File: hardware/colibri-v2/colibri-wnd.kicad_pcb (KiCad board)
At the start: 4 copper layers, 120 x 120 mm, 527 parts, among them CN1 XT60-M, CN10 629_105_150_921, CN11 629_105_150_921, CN12 XT60-F, CN2 XT60-F, CN3 AS0B821-S78B-7H, CN4 HDMI_A, CN5 692_121_030_100, CN6 Wurth-68715014522-LCD, CN7 MOLEX_73366_0061, CN8 629_105_150_921, CN9 Wurth-68711814522, CON1 PJ-102AH, P1 CONN_02X10, P10 CONN_01X08, P11 CONN_01X03, P12 CONN_01X03, P13 CONN_01X03, P14 CONN_01X03, P15 CONN_01X03, P16 CONN_01X03, P17 CONN_01X03, P18 CONN_01X03, P19 CONN_01X03, P20 CONN_01X03, P21 CONN_01X03, P22 CONN_01X03, P23 CONN_01X03, P24 CONN_01X03, P25 CONN_01X03, P26 CONN_01X03, P27 CONN_01X03, P28 CONN_01X03, P29 CONN_01X03, P3 CONN_02X01, P30 CONN_01X03, P31 CONN_01X03, P32 CONN_02X10, P33 ECM00870-L, P34 ECM00870-L, P35 STANDOFF, P36 STANDOFF, P37 STANDOFF, P38 STANDOFF, P39 STANDOFF, P4 ECM00870-L, P5 ECM00870-L, P6 CONN_01X08, P7 CONN_01X04, P8 CONN_01X04, P9 CONN_01X04, Q10 PDTC123JU, Q11 PDTA123JU, Q12 IRLML6402TRPBF, Q13 BSS138PW, Q14 PDTA123JU, Q15 BSS138PW, Q16 BSS138PW, Q17 IRLML6402TRPBF, Q3 BSS138PW, Q4 FDMA530PZ, Q5 BSS138PW, Q6 BSS138PW, Q7 BSS138PW, Q8 AP6681GMT-HF-3TR, Q9 FDMA530PZ, SW1 OMRON B3F-1070, SW10 OMRON B3F-1070, SW11 OMRON B3F-1070, SW2 OMRON B3F-1070, SW3 OMRON B3F-1070, SW4 OMRON B3F-1070, SW5 OMRON B3F-1070, SW6 OMRON B3F-1070, SW7 OMRON B3F-1070, SW8 OMRON B3F-1070, SW9 ALPS-SPPJ320600, U1 L3GD20HTR, U10 TPS2065CDBVT, U11 VBUS054CD-FHI-GS08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

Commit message: Work on PCB placement
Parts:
- moved SW10 92.6 mm to (65.0, 140.2), turned to 0 degrees
- moved SW1 10.2 mm to (94.1, 144.8)
- moved SW11 10.2 mm to (85.2, 144.8)
- moved SW5 10.2 mm to (103.0, 144.8)
- moved SW6 10.2 mm to (111.9, 144.8)
- moved U8 4.89 mm to (118.1, 141.0), turned to 0 degrees
- moved C44 3.30 mm to (61.5, 138.8)
- moved DL8 2.54 mm to (57.9, 139.2)
- moved DL9 2.54 mm to (57.9, 141.2)
- moved CN9 1.78 mm to (103.6, 45.1)
- moved U11 1.52 mm to (52.3, 140.7)
- moved U9 1.52 mm to (52.3, 138.2)
- moved C120 1.27 mm to (95.2, 120.0)
- moved C121 1.27 mm to (97.2, 120.0)
- moved R193 1.27 mm to (128.3, 120.0)
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
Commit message: Work on PCB placement
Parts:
- CN1: footprint Sigmadrone:xt60 -> Sigmadrone:xt60-M
- CN12, CN2: footprint Sigmadrone:xt60 -> Sigmadrone:xt60-F
- DL13, DL17, DL18, DL5, DL7, MSD1: moved to F.Cu
- moved MSD1 92.4 mm to (124.2, 45.0), turned to 0 degrees
- moved R36 34.9 mm to (121.7, 80.0), turned to 180 degrees
- moved P7 33.8 mm to (50.3, 116.3)
- moved R35 32.8 mm to (121.7, 78.1), turned to 180 degrees
- moved P8 32.5 mm to (50.3, 118.9)
- moved P9 31.2 mm to (50.3, 121.4)
- moved BT1 31.1 mm to (57.6, 118.0)
- moved R37 30.8 mm to (121.7, 76.2), turned to 180 degrees
- moved R34 28.8 mm to (121.7, 74.3), turned to 180 degrees
- moved U5 27.7 mm to (126.1, 76.8), turned to 180 degrees
- moved C25 26.6 mm to (130.6, 78.1), turned to 0 degrees
- moved C124 23.2 mm to (130.6, 75.6), turned to 0 degrees
- moved R186 17.6 mm to (140.2, 96.0), turned to 0 degrees
- moved R187 16.4 mm to (140.2, 94.0), turned to 0 degrees
- moved R188 15.1 mm to (140.2, 91.9), turned to 0 degrees
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
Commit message: Work on PCB placement
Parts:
- C44, CN6, DL9, R96: moved to F.Cu
- moved R230 95.7 mm to (58.8, 87.9), turned to 270 degrees
- moved R234 93.8 mm to (56.9, 94.9), turned to 270 degrees
- moved R231 93.4 mm to (60.7, 87.9), turned to 270 degrees
- moved R235 91.3 mm to (58.8, 94.9), turned to 270 degrees
- moved R232 91.1 mm to (62.6, 87.9), turned to 270 degrees
- moved R239 90.4 mm to (56.9, 101.9), turned to 270 degrees
- moved R236 88.9 mm to (60.7, 94.9), turned to 270 degrees
- moved R233 88.7 mm to (64.5, 87.9), turned to 270 degrees
- moved R244 88.0 mm to (56.9, 108.8), turned to 270 degrees
- moved R240 87.8 mm to (58.8, 101.9), turned to 270 degrees
- moved R237 86.4 mm to (62.6, 94.9), turned to 270 degrees
- moved R245 85.3 mm to (58.8, 108.8), turned to 270 degrees
- moved R241 85.3 mm to (60.7, 101.9), turned to 270 degrees
- moved R238 84.0 mm to (64.5, 94.9), turned to 270 degrees
- moved R242 82.7 mm to (62.6, 101.9), turned to 270 degrees
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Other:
- board size 120 x 120 mm -> 120 x 110 mm

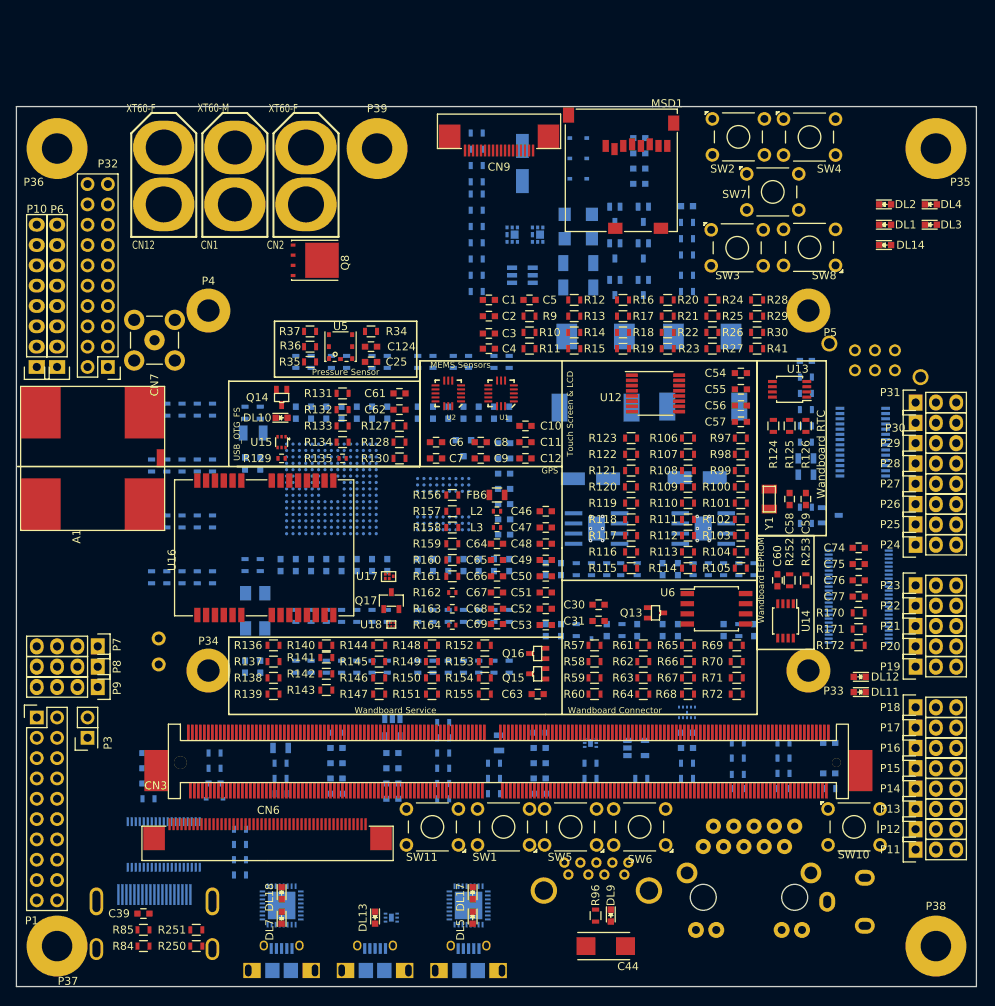
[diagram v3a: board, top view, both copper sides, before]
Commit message: Added one more standoff, next to external sensors
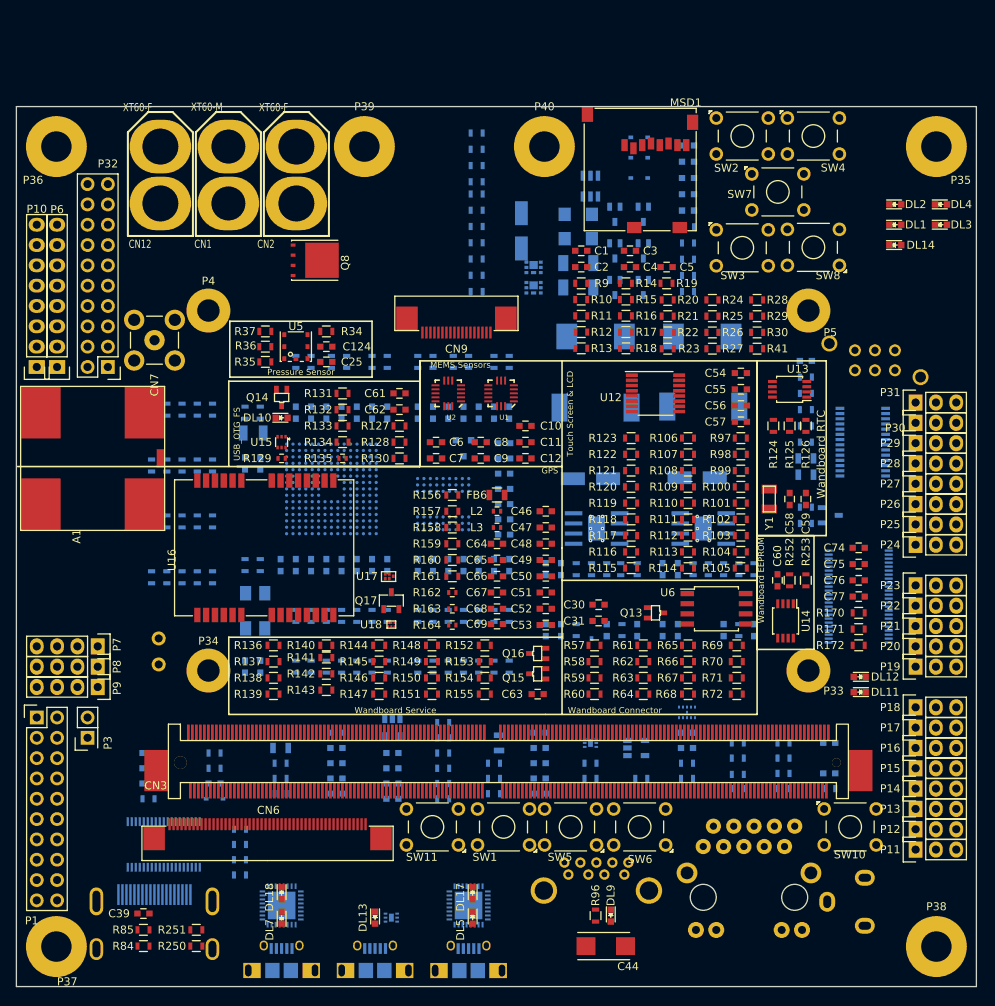
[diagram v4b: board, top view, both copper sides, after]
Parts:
- added P40: STANDOFF, Sigmadrone:STANDOFF-6-32, F.Cu at (106.0, 55.0)
- moved CN9 23.4 mm to (95.0, 78.0)
- moved C3 20.4 mm to (116.7, 68.0)
- moved C4 20.4 mm to (116.7, 70.1)
- moved C5 17.6 mm to (121.3, 70.1)
- moved U27 14.0 mm to (111.8, 59.9), turned to 270 degrees
- moved C1 13.1 mm to (110.6, 68.0)
- moved C2 13.1 mm to (110.6, 70.1)
- moved R19 9.82 mm to (121.3, 72.1)
- moved R14 8.92 mm to (116.2, 72.1)
- moved R15 8.92 mm to (116.2, 74.1)
- moved C27 8.41 mm to (103.1, 65.5)
- moved R10 7.66 mm to (110.6, 74.1)
- moved R9 7.66 mm to (110.6, 72.1)
- moved R11 7.66 mm to (110.6, 76.2)
- moved D3 7.62 mm to (117.9, 53.8)
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
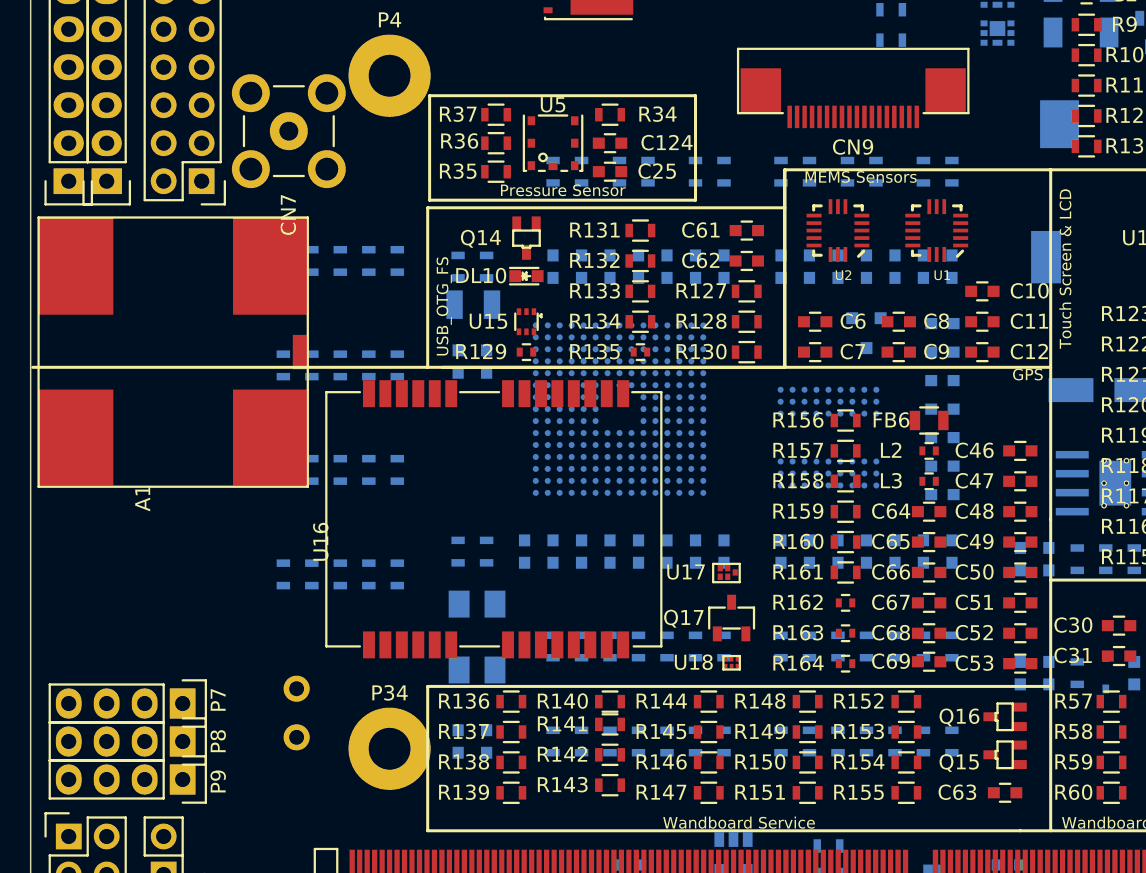
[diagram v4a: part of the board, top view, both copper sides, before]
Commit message: Added design rules and net classes
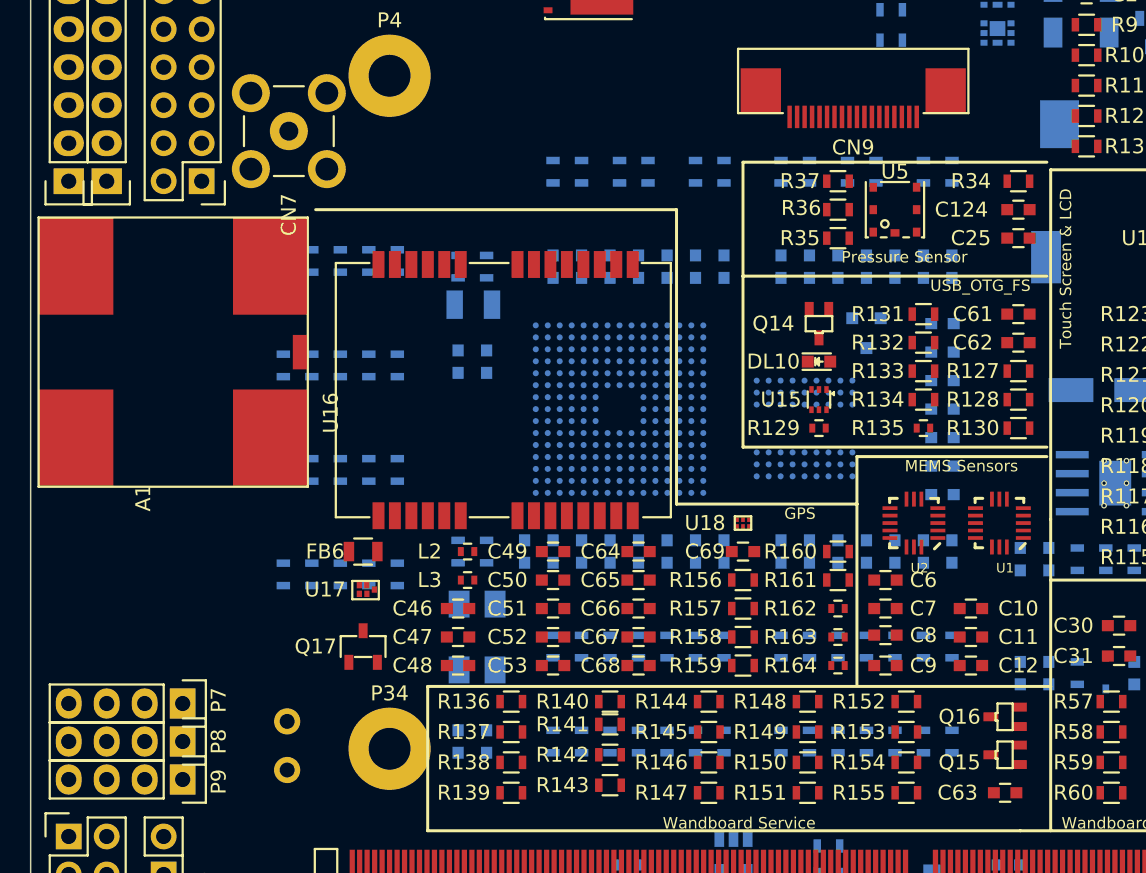
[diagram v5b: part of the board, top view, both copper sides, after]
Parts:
- moved C46 39.0 mm to (68.6, 111.1)
- moved C47 39.0 mm to (68.6, 113.0)
- moved C48 39.0 mm to (68.6, 114.9)
- moved FB6 38.8 mm to (62.2, 107.3)
- moved L2 31.6 mm to (69.2, 107.3)
- moved L3 31.6 mm to (69.2, 109.2)
- moved C49 31.2 mm to (74.9, 107.3)
- moved C50 31.2 mm to (74.9, 109.2)
- moved C51 31.2 mm to (74.9, 111.1)
- moved C52 31.2 mm to (74.9, 113.0)
- moved C53 31.2 mm to (74.9, 114.9)
- moved C124 27.7 mm to (106.0, 84.5), turned to 180 degrees
- moved C25 27.7 mm to (106.0, 86.4), turned to 180 degrees
- moved R34 27.7 mm to (106.0, 82.5), turned to 0 degrees
- moved Q17 24.7 mm to (62.2, 113.7)
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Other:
- net class Default: clearance 0.2 -> 0.12; trace_width 0.25 -> 0.12; via_dia 0.6 -> 0.5; via_drill 0.4 -> 0.35
- net class Power added: clearance 0.3, trace_width 0.8, via_dia 1.3, via_drill 0.8
- net class Signals added: clearance 0.2, trace_width 0.25, via_dia 0.6, via_drill 0.45
- net class TFBGA added: clearance 0.12, trace_width 0.12, via_dia 0.48, via_drill 0.35
- rule trace_clearance: 0.2 -> 0.12
- rule trace_min: 0.2 -> 0.12
- rule via_min_drill: 0.3 -> 0.25

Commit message: Removed net classes. Changed design rules.
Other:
- net class Default: clearance 0.12 -> 0.12192; trace_width 0.12 -> 0.254; via_dia 0.5 -> 0.4826; via_drill 0.35 -> 0.3429
- net class Signals removed
- net class TFBGA removed
- rule trace_clearance: 0.12 -> 0.12192
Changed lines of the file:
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@@
   )
   (setup
-    (last_trace_width 0.12)
+    (last_trace_width 0.254)
     (user_trace_width 0.25)
     (user_trace_width 1.3)
-    (trace_clearance 0.12)
+    (trace_clearance 0.12192)
     (zone_clearance 0.508)
     (zone_45_only no)
@@
     (segment_width 0.2)
     (edge_width 0.1)
-    (via_size 0.5)
-    (via_drill 0.35)
+    (via_size 0.4826)
+    (via_drill 0.3429)
     (via_min_size 0.4)
     (via_min_drill 0.25)
@@
     (uvia_drill 0.1)
     (uvias_allowed no)
-    (uvia_min_size 0.2)
-    (uvia_min_drill 0.1)
+    (uvia_min_size 0)
+    (uvia_min_drill 0)
     (pcb_text_width 0.3)
     (pcb_text_size 1.5 1.5)
@@
   (net 497 "/Servo Motors PWM output/SRV_PWM_0")
   (net_class Default "This is the default net class."
-    (clearance 0.12)
-    (trace_width 0.12)
-    (via_dia 0.5)
-    (via_drill 0.35)
+    (clearance 0.12192)
+    (trace_width 0.254)
+    (via_dia 0.4826)
+    (via_drill 0.3429)
     (uvia_dia 0.3)
     (uvia_drill 0.1)
@@
     (add_net "/Power Control/VH_CTRL")
     (add_net "/Power Control/Vsys")
+    (add_net "/STM32F4 SDRAM/FMC_A0")
+    (add_net "/STM32F4 SDRAM/FMC_A1")
+    (add_net "/STM32F4 SDRAM/FMC_A10")
+    (add_net "/STM32F4 SDRAM/FMC_A11")
+    (add_net "/STM32F4 SDRAM/FMC_A2")
+    (add_net "/STM32F4 SDRAM/FMC_A3")
+    (add_net "/STM32F4 SDRAM/FMC_A4")
+    (add_net "/STM32F4 SDRAM/FMC_A5")
+    (add_net "/STM32F4 SDRAM/FMC_A6")
+    (add_net "/STM32F4 SDRAM/FMC_A7")
+    (add_net "/STM32F4 SDRAM/FMC_A8")
+    (add_net "/STM32F4 SDRAM/FMC_A9")
+    (add_net "/STM32F4 SDRAM/FMC_B0")
+    (add_net "/STM32F4 SDRAM/FMC_B1")
+    (add_net "/STM32F4 SDRAM/FMC_D0")
+    (add_net "/STM32F4 SDRAM/FMC_D1")
+    (add_net "/STM32F4 SDRAM/FMC_D10")
+    (add_net "/STM32F4 SDRAM/FMC_D11")
+    (add_net "/STM32F4 SDRAM/FMC_D12")
+    (add_net "/STM32F4 SDRAM/FMC_D13")
+    (add_net "/STM32F4 SDRAM/FMC_D14")
+    (add_net "/STM32F4 SDRAM/FMC_D15")
+    (add_net "/STM32F4 SDRAM/FMC_D2")
+    (add_net "/STM32F4 SDRAM/FMC_D3")
+    (add_net "/STM32F4 SDRAM/FMC_D4")
+    (add_net "/STM32F4 SDRAM/FMC_D5")
+    (add_net "/STM32F4 SDRAM/FMC_D6")
+    (add_net "/STM32F4 SDRAM/FMC_D7")
+    (add_net "/STM32F4 SDRAM/FMC_D8")
+    (add_net "/STM32F4 SDRAM/FMC_D9")
+    (add_net "/STM32F4 SDRAM/FMC_NBL0")
+    (add_net "/STM32F4 SDRAM/FMC_NBL1")
+    (add_net "/STM32F4 SDRAM/FMC_SDCKE0")
+    (add_net "/STM32F4 SDRAM/FMC_SDCLK")
+    (add_net "/STM32F4 SDRAM/FMC_SDNCAS")
+    (add_net "/STM32F4 SDRAM/FMC_SDNE0")
+    (add_net "/STM32F4 SDRAM/FMC_SDNRAS")
+    (add_net "/STM32F4 SDRAM/FMC_SDNWE")
     (add_net "/Sensors Power Control/V_SENS_CTRL")
     (add_net "/Servo Motors PWM output/SRV_PWM_0")
@@
     (add_net "/Wandboard Connector/Wandboard USB Host/USB_HOST_DP")
     (add_net "/Wandboard Connector/Wandboard USB Host/USB_HOST_OC")
+    (add_net /cortex/C_OTG_FS_OC)
+    (add_net /cortex/C_OTG_FS_PSO)
+    (add_net /cortex/GPS_PWR_CTRL)
+    (add_net /cortex/GPS_RXD)
+    (add_net /cortex/IN_PWM_01)
+    (add_net /cortex/IN_PWM_02)
+    (add_net /cortex/IN_PWM_03)
+    (add_net /cortex/IN_PWM_04)
+    (add_net /cortex/IN_PWM_05)
+    (add_net /cortex/MEMS_ACC_CS)
+    (add_net /cortex/MEMS_GYRO_CS)
+    (add_net /cortex/MEMS_SPI5_MISO)
+    (add_net /cortex/MEMS_SPI5_MOSI)
+    (add_net /cortex/MEMS_SPI5_SCK)
+    (add_net /cortex/OSC-IN)
+    (add_net /cortex/OSC-OUT)
+    (add_net /cortex/OTG_HS_DM)
+    (add_net /cortex/OTG_HS_DP)
+    (add_net /cortex/OTG_HS_VBUS)
+    (add_net /cortex/PCA9685_OE)
+    (add_net /cortex/PCA9685_SCL)
+    (add_net /cortex/PCA9685_SDA)
+    (add_net /cortex/PF6)
+    (add_net /cortex/PH0)
+    (add_net /cortex/PH1)
+    (add_net /cortex/PH12)
+    (add_net /cortex/PH13)
+    (add_net /cortex/PH14)
+    (add_net /cortex/PH15)
+    (add_net /cortex/PH6)
+    (add_net /cortex/PI10)
+    (add_net /cortex/PI6)
+    (add_net /cortex/PI7)
+    (add_net /cortex/PI8)
+    (add_net /cortex/PI9)
+    (add_net /cortex/PS_I2C1_SCL)
+    (add_net /cortex/PS_I2C1_SDA)
+    (add_net /cortex/PWM_SRV_EN)
+    (add_net /cortex/SPI4_MISO)
+    (add_net /cortex/SPI4_MOSI)
+    (add_net /cortex/TIM1_CH2/FMC_D8)
+    (add_net /cortex/TIM1_CH2/OTG_FS_VBUS)
+    (add_net /cortex/TIM1_CH3/FMC_D10)
+    (add_net /cortex/TIM1_CH3/OTG_FS_ID)
+    (add_net /cortex/TIM1_CH4/FMC_D11)
+    (add_net /cortex/TIM1_CH4/OTG_FS_DM)
+    (add_net /cortex/USART2_CTS)
+    (add_net /cortex/USART2_RTS)
+    (add_net /cortex/VCAP1)
+    (add_net /cortex/VCAP2)
+    (add_net /cortex/WB_UART_RX)
     (add_net GND)
     (add_net "Net-(A1-Pad1)")
@@
     (add_net +BATT)
   )
-  (net_class Signals ""
-    (clearance 0.2)
-    (trace_width 0.25)
-    (via_dia 0.6)
-    (via_drill 0.45)
-    (uvia_dia 0.3)
-    (uvia_drill 0.1)
-  )
-  (net_class TFBGA ""
-    (clearance 0.12)
-    (trace_width 0.12)
-    (via_dia 0.48)
-    (via_drill 0.35)
-    (uvia_dia 0.3)
-    (uvia_drill 0.1)
-    (add_net "/STM32F4 SDRAM/FMC_A0")
-    (add_net "/STM32F4 SDRAM/FMC_A1")
-    (add_net "/STM32F4 SDRAM/FMC_A10")
-    (add_net "/STM32F4 SDRAM/FMC_A11")
-    (add_net "/STM32F4 SDRAM/FMC_A2")
-    (add_net "/STM32F4 SDRAM/FMC_A3")
-    (add_net "/STM32F4 SDRAM/FMC_A4")
-    (add_net "/STM32F4 SDRAM/FMC_A5")
-    (add_net "/STM32F4 SDRAM/FMC_A6")
-    (add_net "/STM32F4 SDRAM/FMC_A7")
-    (add_net "/STM32F4 SDRAM/FMC_A8")
-    (add_net "/STM32F4 SDRAM/FMC_A9")
-    (add_net "/STM32F4 SDRAM/FMC_B0")
-    (add_net "/STM32F4 SDRAM/FMC_B1")
-    (add_net "/STM32F4 SDRAM/FMC_D0")
-    (add_net "/STM32F4 SDRAM/FMC_D1")
-    (add_net "/STM32F4 SDRAM/FMC_D10")
-    (add_net "/STM32F4 SDRAM/FMC_D11")
-    (add_net "/STM32F4 SDRAM/FMC_D12")
-    (add_net "/STM32F4 SDRAM/FMC_D13")
-    (add_net "/STM32F4 SDRAM/FMC_D14")
-    (add_net "/STM32F4 SDRAM/FMC_D15")
-    (add_net "/STM32F4 SDRAM/FMC_D2")
-    (add_net "/STM32F4 SDRAM/FMC_D3")
-    (add_net "/STM32F4 SDRAM/FMC_D4")
-    (add_net "/STM32F4 SDRAM/FMC_D5")
-    (add_net "/STM32F4 SDRAM/FMC_D6")
-    (add_net "/STM32F4 SDRAM/FMC_D7")
-    (add_net "/STM32F4 SDRAM/FMC_D8")
-    (add_net "/STM32F4 SDRAM/FMC_D9")
-    (add_net "/STM32F4 SDRAM/FMC_NBL0")
-    (add_net "/STM32F4 SDRAM/FMC_NBL1")
-    (add_net "/STM32F4 SDRAM/FMC_SDCKE0")
-    (add_net "/STM32F4 SDRAM/FMC_SDCLK")
-    (add_net "/STM32F4 SDRAM/FMC_SDNCAS")
-    (add_net "/STM32F4 SDRAM/FMC_SDNE0")
-    (add_net "/STM32F4 SDRAM/FMC_SDNRAS")
-    (add_net "/STM32F4 SDRAM/FMC_SDNWE")
-    (add_net /cortex/C_OTG_FS_OC)
-    (add_net /cortex/C_OTG_FS_PSO)
-    (add_net /cortex/GPS_PWR_CTRL)
-    (add_net /cortex/GPS_RXD)
-    (add_net /cortex/IN_PWM_01)
-    (add_net /cortex/IN_PWM_02)
-    (add_net /cortex/IN_PWM_03)
-    (add_net /cortex/IN_PWM_04)
-    (add_net /cortex/IN_PWM_05)
-    (add_net /cortex/MEMS_ACC_CS)
-    (add_net /cortex/MEMS_GYRO_CS)
-    (add_net /cortex/MEMS_SPI5_MISO)
-    (add_net /cortex/MEMS_SPI5_MOSI)
-    (add_net /cortex/MEMS_SPI5_SCK)
-    (add_net /cortex/OSC-IN)
-    (add_net /cortex/OSC-OUT)
-    (add_net /cortex/OTG_HS_DM)
-    (add_net /cortex/OTG_HS_DP)
-    (add_net /cortex/OTG_HS_VBUS)
-    (add_net /cortex/PCA9685_OE)
-    (add_net /cortex/PCA9685_SCL)
-    (add_net /cortex/PCA9685_SDA)
-    (add_net /cortex/PF6)
-    (add_net /cortex/PH0)
-    (add_net /cortex/PH1)
-    (add_net /cortex/PH12)
-    (add_net /cortex/PH13)
-    (add_net /cortex/PH14)
-    (add_net /cortex/PH15)
-    (add_net /cortex/PH6)
-    (add_net /cortex/PI10)
-    (add_net /cortex/PI6)
-    (add_net /cortex/PI7)
-    (add_net /cortex/PI8)
-    (add_net /cortex/PI9)
-    (add_net /cortex/PS_I2C1_SCL)
-    (add_net /cortex/PS_I2C1_SDA)
-    (add_net /cortex/PWM_SRV_EN)
-    (add_net /cortex/SPI4_MISO)
-    (add_net /cortex/SPI4_MOSI)
-    (add_net /cortex/TIM1_CH2/FMC_D8)
-    (add_net /cortex/TIM1_CH2/OTG_FS_VBUS)
-    (add_net /cortex/TIM1_CH3/FMC_D10)
-    (add_net /cortex/TIM1_CH3/OTG_FS_ID)
-    (add_net /cortex/TIM1_CH4/FMC_D11)
-    (add_net /cortex/TIM1_CH4/OTG_FS_DM)
-    (add_net /cortex/USART2_CTS)
-    (add_net /cortex/USART2_RTS)
-    (add_net /cortex/VCAP1)
-    (add_net /cortex/VCAP2)
-    (add_net /cortex/WB_UART_RX)
-  )
   (module Sigmadrone:STANDOFF-6-32 (layer F.Cu)
